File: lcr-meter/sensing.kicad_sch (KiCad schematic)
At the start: 0 parts

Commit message: Progress, removal of unnecessary components
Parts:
- added J4: Conn_01x04, symbol Connector_Generic:Conn_01x04
- added R2: R, symbol Device:R
- added U10, U15: AD8216, Package_SO:SOIC-8_3.9x4.9mm_P1.27mm, symbol Amplifier_Current:AD8216
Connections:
- new net +5V: U10.6 (V+), U15.6 (V+)
- new net GND: R2.2, U10.1 (-IN), U10.2 (GND), U10.3 (Vref2), U10.7 (Vref1), U15.2 (GND), U15.3 (Vref2), U15.7 (Vref1)
- new net I_LOAD: J4.1 (Pin_1)
- new net I_SHUNT: J4.2 (Pin_2), R2.1, U10.8 (+IN)
- new net SHUNT_SENSE: U10.5 (OUT)
- new net V_SENSE: U15.5 (OUT)
- new net V_SENSE+: J4.3 (Pin_3), U15.8 (+IN)
- new net V_SENSE-: J4.4 (Pin_4), U15.1 (-IN)
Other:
- note added: "Sensing kelvin connection"

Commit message: Breadboarding notes
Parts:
- added R3, R6: R_Small, symbol Device:R_Small
- added U2: AD8216, Package_SO:SOIC-8_3.9x4.9mm_P1.27mm, symbol Amplifier_Current:AD8216
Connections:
- net +5V: now also U2.6 (V+)
- net GND: now also R6.2, U2.2 (GND), U2.3 (Vref2), U2.7 (Vref1)
- net SHUNT_SENSE: now also R3.2, R6.1; no longer U10.5 (OUT)
- net I_SHUNT renamed SHUNT+
- new net: U10.5 (OUT), U2.1 (-IN)
- new net: R3.1, U2.5 (OUT)
- new net +1V8: U2.8 (+IN)
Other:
- note added: "In testing - AMP03"
- moved on the sheet: R2, U10

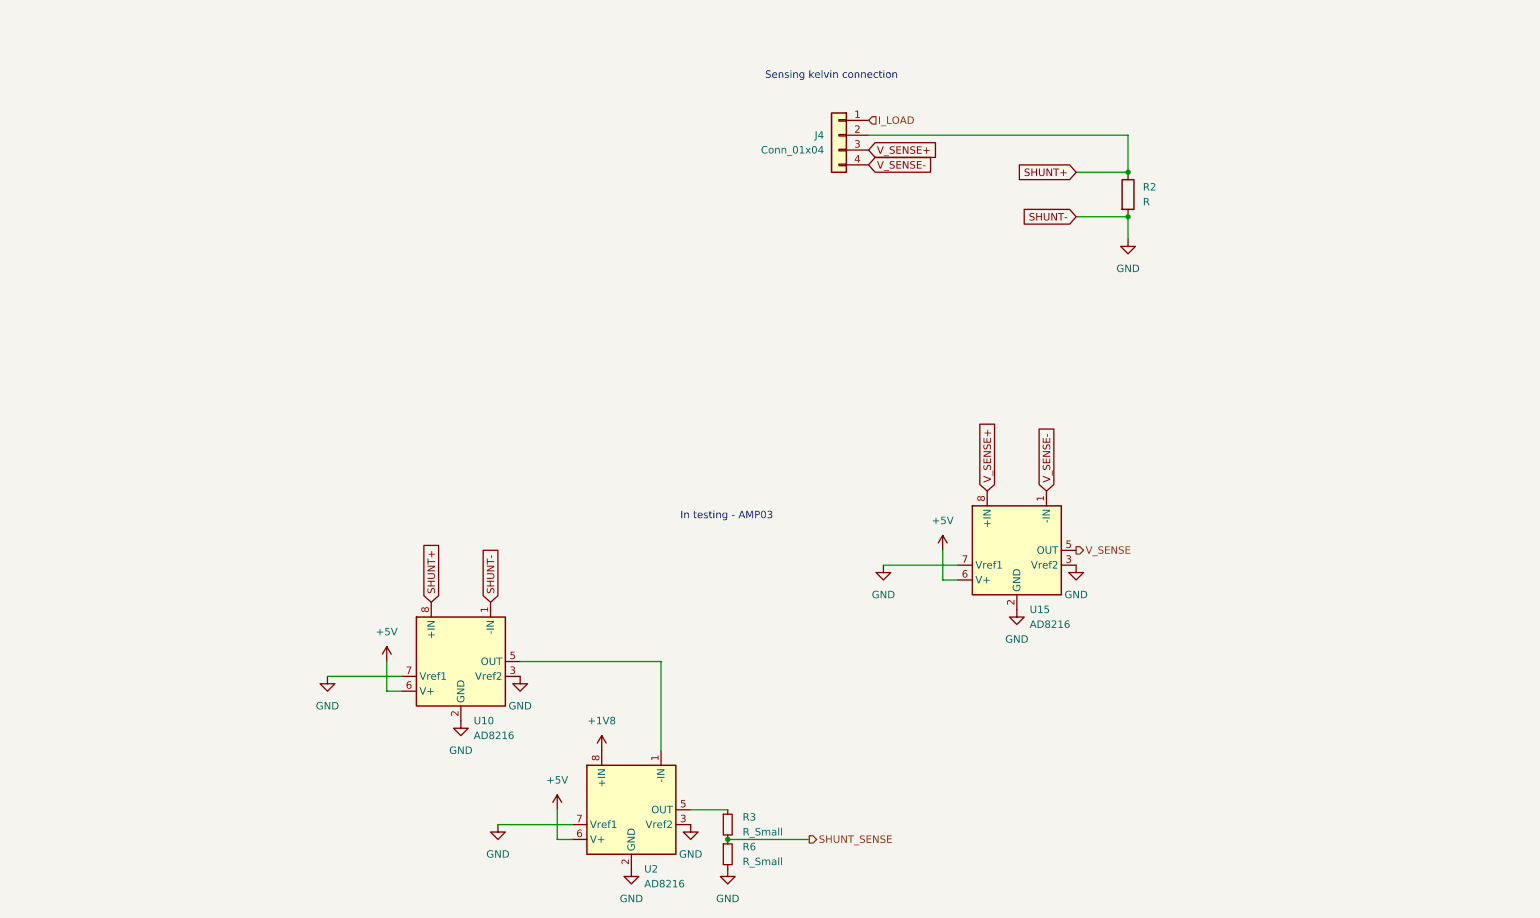
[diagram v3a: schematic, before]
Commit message: Schematic updates, added -5V, finalized sensing
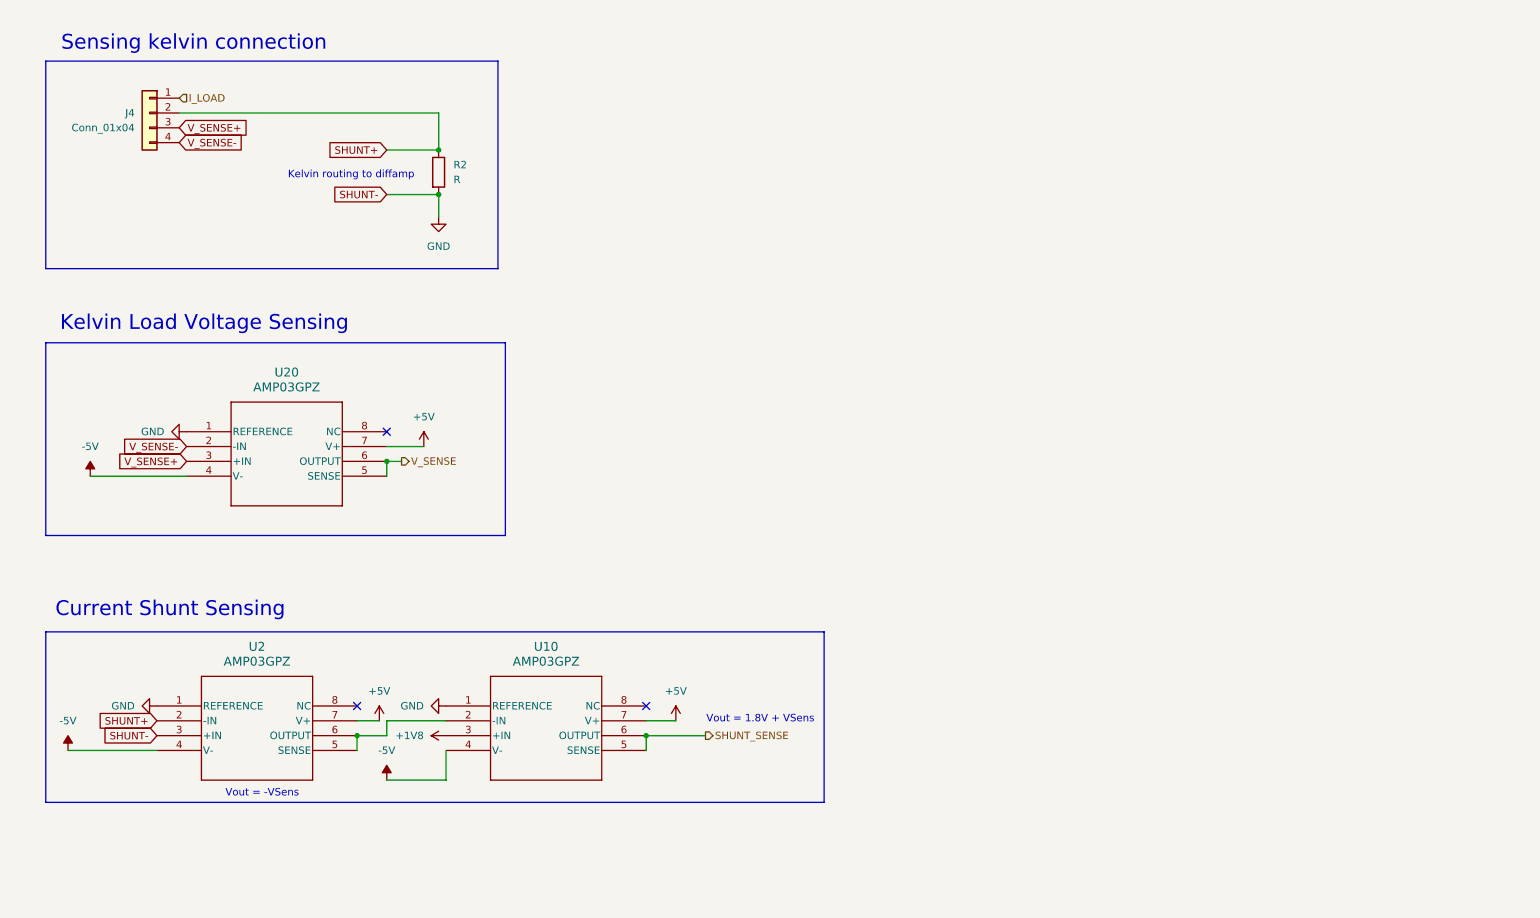
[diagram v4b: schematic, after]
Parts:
- removed R3, R6: R_Small, symbol Device:R_Small
- removed U10, U15, U2: AD8216, Package_SO:SOIC-8_3.9x4.9mm_P1.27mm, symbol Amplifier_Current:AD8216
- added U10, U2, U20: AMP03GPZ, N_8_ADI, symbol 2024-10-13_10-13-09:AMP03GPZ
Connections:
- net +1V8: now also U10.3 (+IN)
- net +5V: now also U10.7 (V+), U2.7 (V+), U20.7 (V+)
- net GND: now also U10.1 (REFERENCE), U2.1 (REFERENCE), U2.3 (+IN), U20.1 (REFERENCE)
- net SHUNT+: now also U2.2 (-IN)
- net SHUNT_SENSE: now also U10.5 (SENSE), U10.6 (OUTPUT)
- net V_SENSE: now also U20.5 (SENSE), U20.6 (OUTPUT)
- net V_SENSE+: now also U20.3 (+IN)
- net V_SENSE-: now also U20.2 (-IN)
- new net: U10.2 (-IN), U2.5 (SENSE), U2.6 (OUTPUT)
- new net -5V: U10.4 (V-), U2.4 (V-), U20.4 (V-)
- no-connect marks 0 -> 3
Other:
- note added: "Current Shunt Sensing"
- note added: "Kelvin Load Voltage Sensing"
- note added: "Kelvin routing to diffamp"
- note added: "Vout = -VSens"
- note added: "Vout = 1.8V + VSens"
- note removed: "In testing - AMP03"
- moved on the sheet: J4, R2

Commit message: Schematic polishing, starting MCU schematic
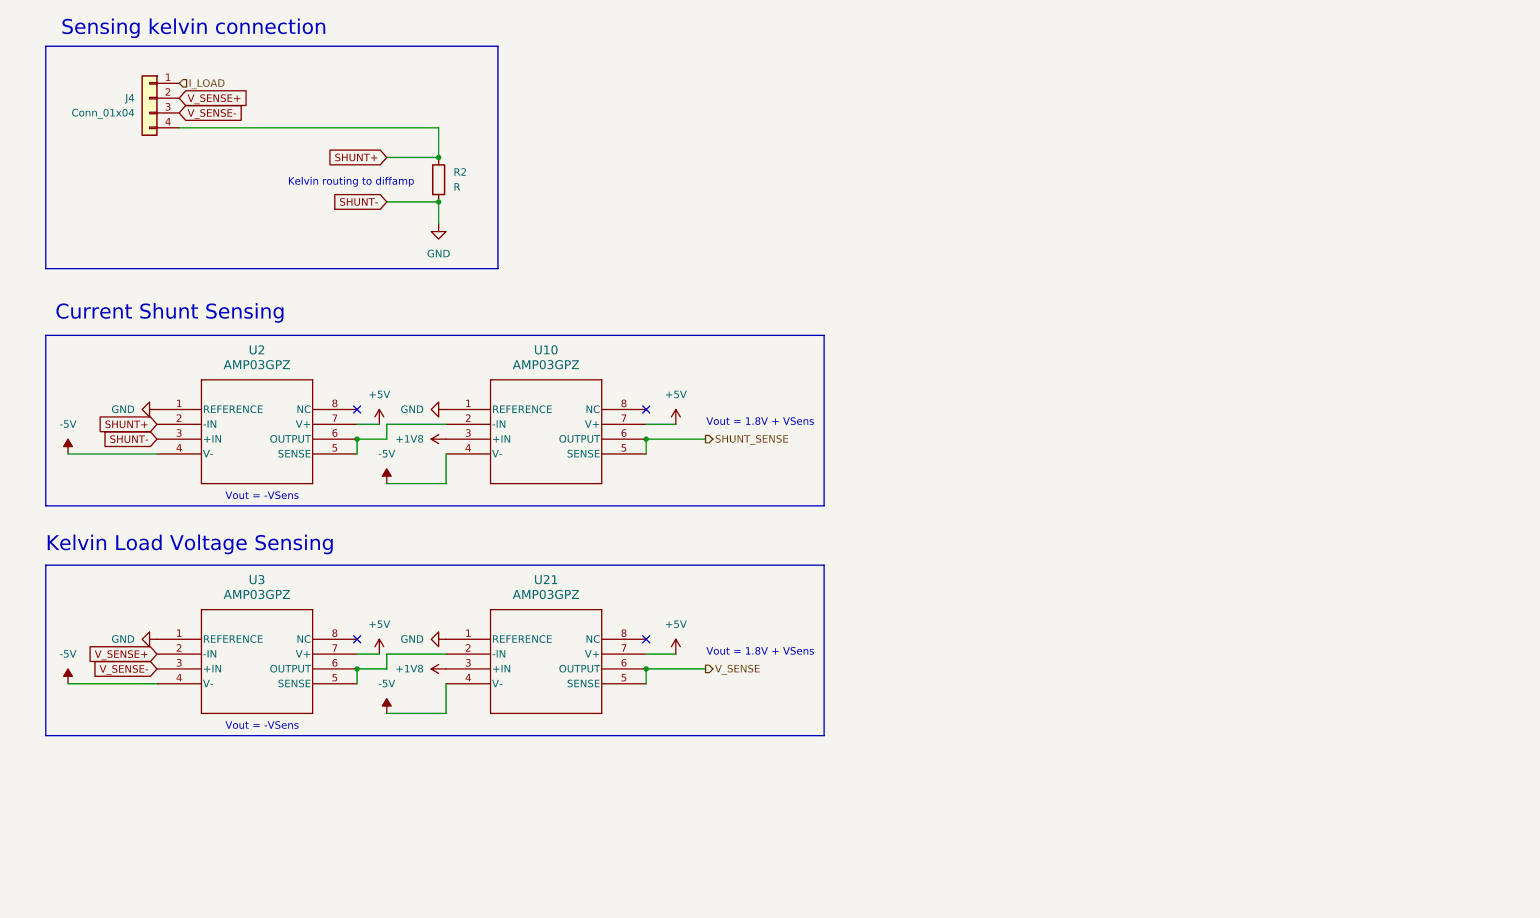
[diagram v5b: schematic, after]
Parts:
- removed U20: AMP03GPZ, N_8_ADI, symbol 2024-10-13_10-13-09:AMP03GPZ
- added U21, U3: AMP03GPZ, N_8_ADI, symbol 2024-10-13_10-13-09:AMP03GPZ
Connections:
- net +1V8: now also U21.3 (+IN)
- net +5V: now also U21.7 (V+), U3.7 (V+)
- net -5V: now also U21.4 (V-), U3.4 (V-)
- net GND: now also U21.1 (REFERENCE), U3.1 (REFERENCE)
- net SHUNT+: now also J4.4 (Pin_4); no longer J4.2 (Pin_2)
- net V_SENSE: now also U21.5 (SENSE), U21.6 (OUTPUT)
- net V_SENSE+: now also J4.2 (Pin_2), U3.2 (-IN); no longer J4.3 (Pin_3)
- net V_SENSE-: now also J4.3 (Pin_3), U3.3 (+IN); no longer J4.4 (Pin_4)
- new net: U21.2 (-IN), U3.5 (SENSE), U3.6 (OUTPUT)
- no-connect marks 3 -> 4
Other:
- moved on the sheet: J4, R2, U10, U2

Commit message: Schematic completion
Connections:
- net SHUNT+ renamed Shunt+
- net V_SENSE+ renamed V_Sense+
- net V_SENSE- renamed V_Sense-

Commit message: Schematic polishing
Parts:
- removed R2: R, symbol Device:R
- added C22, C23, C24, C46, C54, C55, C56, C62, C63, C64, C65, C66: 100n, Capacitor_SMD:C_0402_1005Metric, symbol Device:C_Small
- added C67, C69, C71: 2.2u, Capacitor_SMD:C_0402_1005Metric, symbol Device:C_Small
- added C68, C70, C72: 4.7u, Capacitor_SMD:C_0402_1005Metric, symbol Device:C_Small
- added D1, D2: SP0502BAJT, Package_TO_SOT_SMD:SOT-323_SC-70, symbol Power_Protection:SP0502BAJT
- added R15: 100R, Resistor_SMD:R_0402_1005Metric, symbol Device:R_Small
- added R16: 1k, Resistor_SMD:R_0402_1005Metric, symbol Device:R_Small
- added R17: 10k, Resistor_SMD:R_0402_1005Metric, symbol Device:R_Small
- added R18: 100k, Resistor_SMD:R_0402_1005Metric, symbol Device:R_Small
- added U11, U12, U8, U9: TMUX1101DCK, Package_TO_SOT_SMD:SOT-23-5, symbol Analog_Switch:TMUX1101DCK
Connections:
- net +5V: now also C54.1, C55.1, C56.1, C62.1, C69.1, C70.1
- net -5V: now also C63.1, C64.1, C65.1, C66.1, C71.1, C72.1
- net GND: now also C22.2, C23.2, C24.2, C46.2, C54.2, C55.2, C56.2, C62.2, C63.2, C64.2, C65.2, C66.2, C67.2, C68.2, C69.2, C70.2, C71.2, C72.2, D1.3 (A), D2.3 (A), U11.1, U11.3 (GND), U12.1, U12.3 (GND), U8.1, U8.3 (GND), U9.1, U9.3 (GND)
- net I_LOAD: now also D1.1 (K)
- net V_Sense+: now also D1.2 (K)
- net V_Sense-: now also D2.1 (K)
- net Shunt+ renamed I_In
- net I_In: now also D2.2 (K), R15.1, R16.1, R17.1, R18.1
- new net: R15.2, U8.2
- new net: R18.2, U12.2
- new net: R16.2, U9.2
- new net: R17.2, U11.2
- new net +3V3: C22.1, C23.1, C24.1, C46.1, C67.1, C68.1, U11.5 (V_{DD}), U12.5 (V_{DD}), U8.5 (V_{DD}), U9.5 (V_{DD})
- new net RANGE_0: U8.4
- new net RANGE_1: U9.4
- new net RANGE_2: U11.4
- new net RANGE_3: U12.4
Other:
- note added: "Input Protection"
- note added: "Make sure to have good common mode current isolation for these"
- note added: "Most of these may not be needed, just here to help PSRR. 3.3V caps are more critical here for the analog switches."
- note added: "Range Resistor Switches"
- note added: "Supply Decoupling"
- note added: "Switch decoupling"
- note removed: "Kelvin routing to diffamp"
- moved on the sheet: U10, U2, U21, U3

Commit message: Schematic polishing
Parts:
- C68, C70, C72: footprint Capacitor_SMD:C_0402_1005Metric -> Capacitor_SMD:C_0805_2012Metric
- J4: footprint (none) -> Connector_PinHeader_2.54mm:PinHeader_1x04_P2.54mm_Vertical
- U10, U2, U21, U3: footprint N_8_ADI -> footprints:N_8_ADI
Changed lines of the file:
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@@
 			)
 		)
-		(property "Footprint" "N_8_ADI"
+		(property "Footprint" "footprints:N_8_ADI"
 			(at 41.91 144.78 0)
 			(effects
@@
 			)
 		)
-		(property "Footprint" "Capacitor_SMD:C_0402_1005Metric"
+		(property "Footprint" "Capacitor_SMD:C_0805_2012Metric"
 			(at 217.17 63.5 0)
 			(effects
@@
 			)
 		)
-		(property "Footprint" "N_8_ADI"
+		(property "Footprint" "footprints:N_8_ADI"
 			(at 91.44 105.41 0)
 			(effects
@@
 			)
 		)
-		(property "Footprint" ""
+		(property "Footprint" "Connector_PinHeader_2.54mm:PinHeader_1x04_P2.54mm_Vertical"
 			(at 40.64 34.29 0)
 			(effects
@@
 			)
 		)
-		(property "Footprint" "N_8_ADI"
+		(property "Footprint" "footprints:N_8_ADI"
 			(at 41.91 105.41 0)
 			(effects
@@
 			)
 		)
-		(property "Footprint" "Capacitor_SMD:C_0402_1005Metric"
+		(property "Footprint" "Capacitor_SMD:C_0805_2012Metric"
 			(at 217.17 49.53 0)
 			(effects
@@
 			)
 		)
-		(property "Footprint" "Capacitor_SMD:C_0402_1005Metric"
+		(property "Footprint" "Capacitor_SMD:C_0805_2012Metric"
 			(at 217.17 35.56 0)
 			(effects
@@
 			)
 		)
-		(property "Footprint" "N_8_ADI"
+		(property "Footprint" "footprints:N_8_ADI"
 			(at 91.44 144.78 0)
 			(effects
